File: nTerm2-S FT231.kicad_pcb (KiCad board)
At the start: 2 copper layers, 147.3 x 55.9 mm, 126 parts, among them J1 VGA, J2 Keyboard, J3 Mouse, J4 Line-out/Speaker, J5 RS-232 V.24, J6 USB_C_Receptacle_USB2.0_16P, J7 Line-out/Speaker, K1 IM41 3V, K2 IM41 3V, K3 IM41 3V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

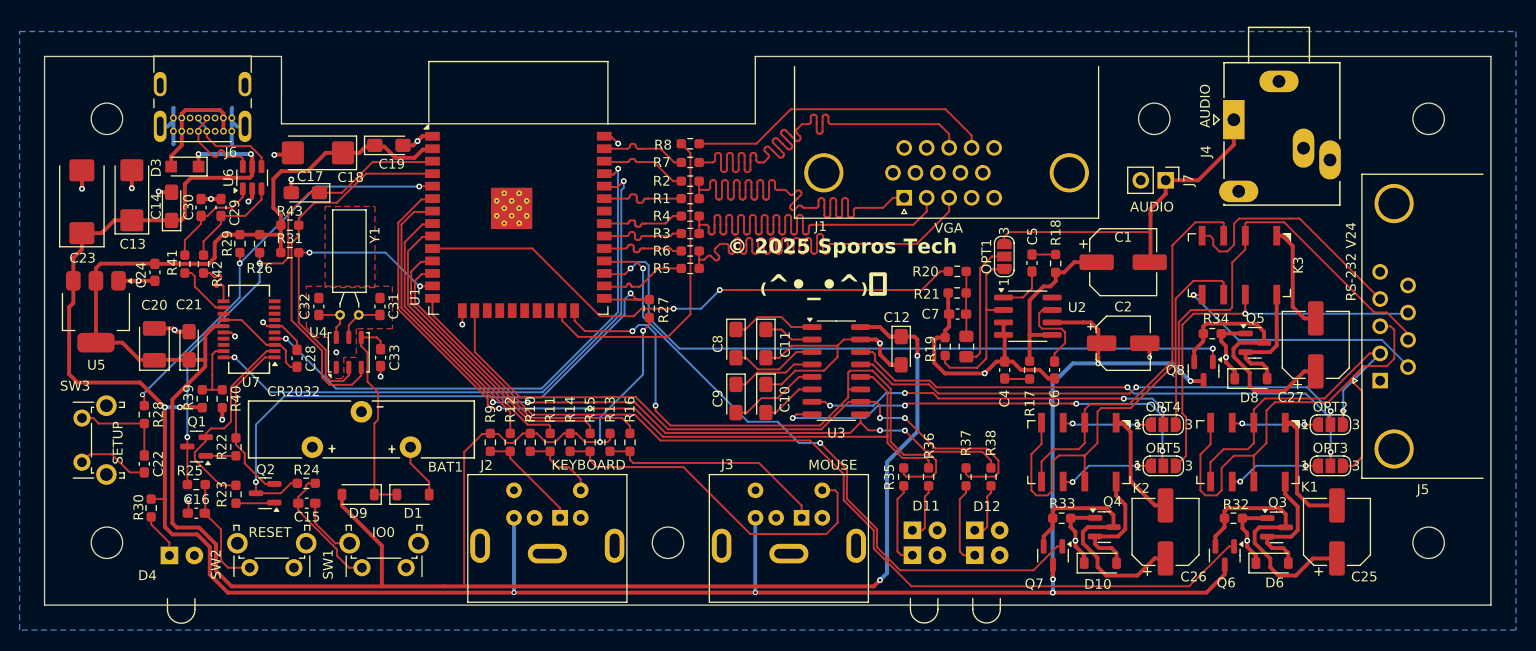
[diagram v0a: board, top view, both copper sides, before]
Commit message: V0.10 small detail fixes. - Rotate C19 180 degrees, so that it's oriented as the rest of the caps. - Tweak the positions of several connectors and LEDs so that they are flush with the PCB edge. - Connect pins 2 and 3 (both +) of the battery housing together so that it doesn't matter anymore to which hole you solder the + wire.
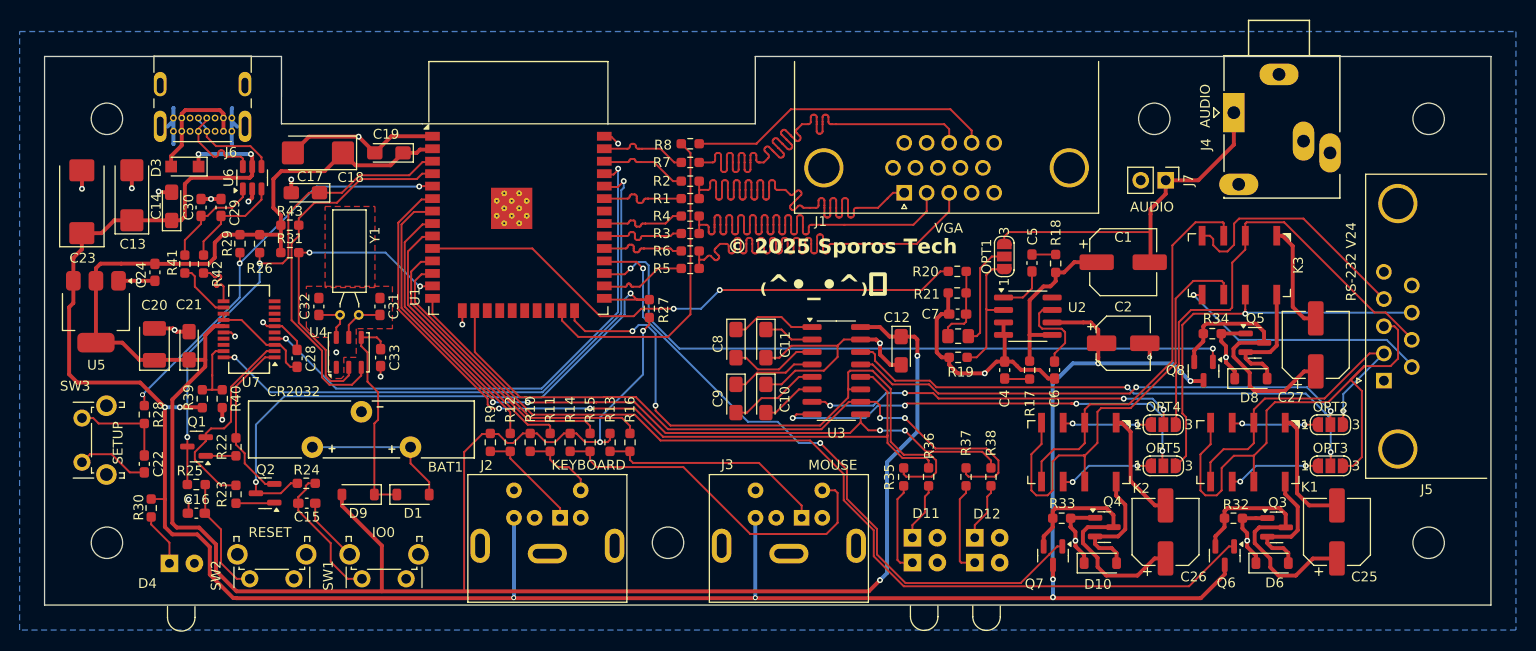
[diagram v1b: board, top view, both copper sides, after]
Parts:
- moved R19 1.72 mm to (167.2, 102.6), turned to 0 degrees
- moved C3 1.35 mm to (167.2, 100.5), turned to 0 degrees
- moved SW1 1.13 mm to (110.9, 125.2)
- moved SW2 1.13 mm to (99.5, 125.2)
- moved D4 0.80 mm to (86.8, 123.6)
- moved C19 0.76 mm to (109.2, 81.8), turned to 180 degrees
- moved D11 0.76 mm to (162.5, 121.0)
- moved D12 0.76 mm to (168.8, 121.0)
- moved J4 0.72 mm to (195.2, 77.7)
- moved J1 0.51 mm to (161.7, 84.7)
- moved J5 0.38 mm to (210.5, 105.0)
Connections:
- BAT1 pad 3: unconnected-(BAT1-Pad3) -> Net-(D1-A)
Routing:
- net GND: track 136.6 -> 146.9 mm, vias 24 -> 23
- net Net-(D1-A): track 5.62 -> 15.6 mm
- net Net-(OPT1-A): track 17.8 -> 13.5 mm
- net Net-(OPT1-C): track 13.1 -> 10.9 mm
- net +5V: track 249.3 -> 251.3 mm
- net Net-(C3-Pad1): track 6.61 -> 8.38 mm
- net +3V3: track 257.5 -> 259.0 mm
- net REVERSE_RTS_CTS_DTR_DSR: track 66.4 -> 67.9 mm
- net Net-(C15-Pad1): track 13.2 -> 14.4 mm
- net Net-(D12-A2): track 8.63 -> 9.53 mm
- net Net-(D11-A2): track 8.63 -> 9.45 mm
- net /_RXD: track 33.9 -> 34.6 mm
- net Net-(J7-Pin_1): track 35.8 -> 36.5 mm
- net Net-(D4-A): track 4.96 -> 5.65 mm
- net Net-(C16-Pad1): track 11.7 -> 12.3 mm
